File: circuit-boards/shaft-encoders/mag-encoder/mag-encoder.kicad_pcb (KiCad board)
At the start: 4 copper layers, 26.7 x 31.8 mm, 23 parts, among them J1 0015912055, J2 CONFIG, U1 AP2120N-3.3TRG1, U2 SN74LVC1G02DBVR, U3 MA732GQ

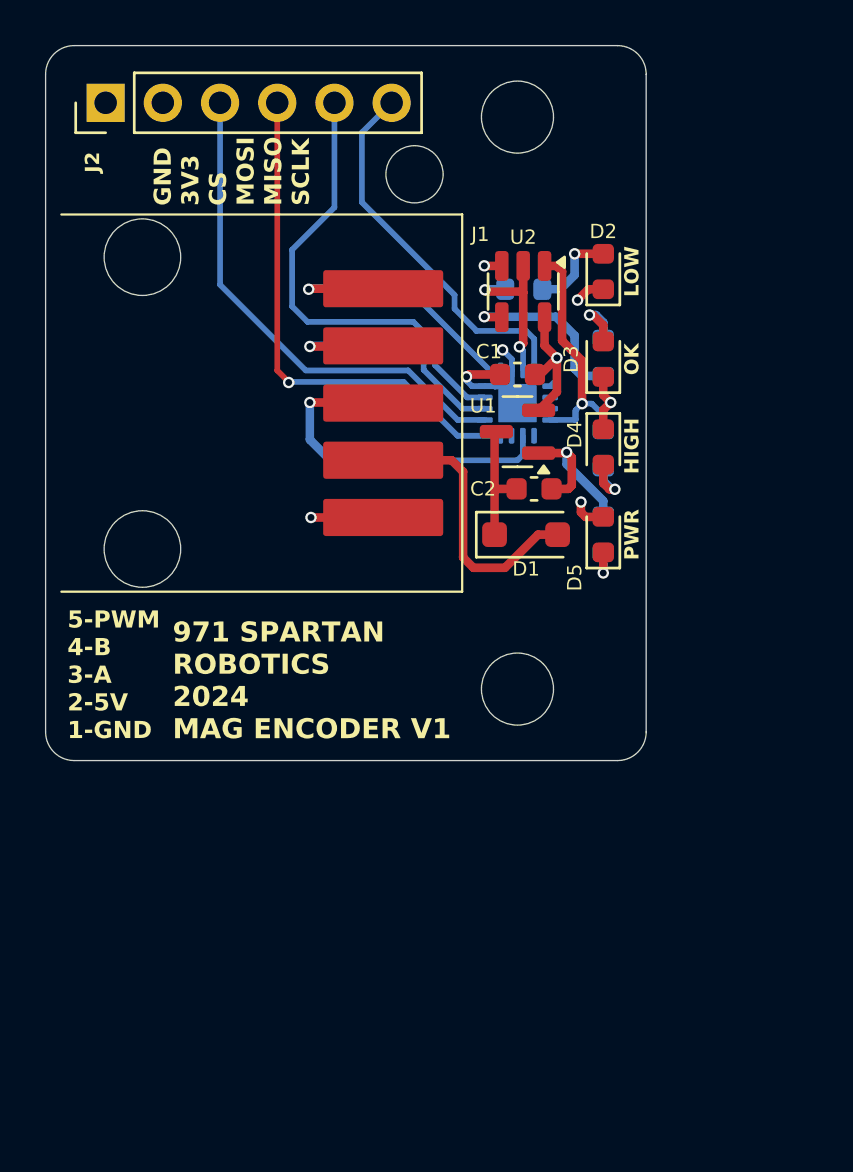
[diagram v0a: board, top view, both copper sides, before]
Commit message: checkin of mag encoder
Signed-off-by: Scott <sgberman1@gmail.com>
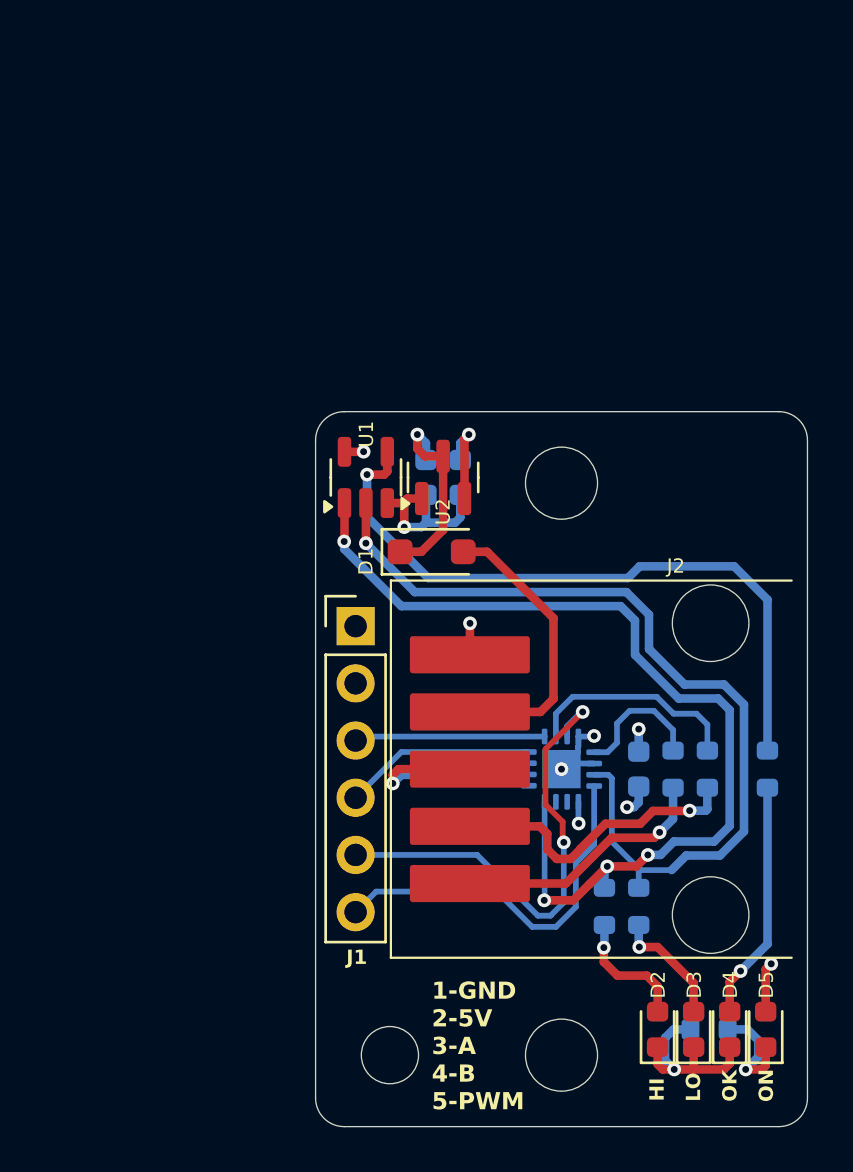
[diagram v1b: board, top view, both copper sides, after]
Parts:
- removed the H4 at (224.0, 117.5)
- removed the R3 at (232.4, 113.1)
- added C1: 1uF-10%-25V-0603, Capacitor_SMD:C_0603_1608Metric, B.Cu at (226.1, 110.6)
- added H2: Slot, mag-encoder:pin-0.100, F.Cu at (238.2, 110.9)
- added R7: 1.00k-1%-0603, Resistor_SMD:R_0603_1608Metric, B.Cu at (237.1, 135.1)
- C2: moved to B.Cu
- C3: renamed from C1; moved to B.Cu
- D2: renamed from D4; value HIGH -> HI
- D3: renamed from D2; value LOW -> LO
- D5: value PWR -> ON
- moved H4 41.7 mm to (230.6, 136.3), turned to 180 degrees
- moved H3 39.1 mm to (222.9, 136.3)
- moved J2 37.5 mm to (241.5, 123.6), turned to 90 degrees
- moved D3 33.9 mm to (236.4, 135.1)
- moved D4 30.3 mm to (238.0, 135.1)
- moved R5 27.9 mm to (234.0, 129.7), turned to -90 degrees
- moved D2 26.0 mm to (234.8, 135.1), turned to 90 degrees
- moved J1 25.8 mm to (221.4, 117.2), turned to 0 degrees
- moved R3 25.1 mm to (235.5, 123.6), turned to -90 degrees
- moved R2 23.9 mm to (237.0, 123.6), turned to -90 degrees
- moved D5 23.1 mm to (239.6, 135.1)
- moved R6 20.3 mm to (232.5, 129.7)
- moved R1 19.7 mm to (239.7, 123.6), turned to -90 degrees
- moved C3 18.3 mm to (234.0, 123.6), turned to 90 degrees
- moved U3 16.4 mm to (230.6, 123.6), turned to 0 degrees
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- renumbered D3 to D4, H2 to H1, H1 to H4, J2 to J1, J1 to J2, R6 to R2, R5 to R3, R7 to R4, R4 to R5, R2 to R6, U2 to U1, U1 to U2
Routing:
- net Net-(U3-MGL): track 7.45 -> 39.7 mm, vias 2 -> 1
- net Net-(U3-MGH): track 11.3 -> 43.2 mm, vias 1 -> 4
- net Net-(R1-Pad1): track 8.02 -> 30.1 mm
- net /MOSI: track 23.0 -> 8.54 mm, vias 1 -> 0
- net /CS: track 22.3 -> 8.47 mm
- net /B: track 5.32 -> 13.4 mm
- net Net-(D4-A): track 2.99 -> 10.6 mm
- net /PWM: track 5.42 -> 11.6 mm
- net Net-(U3-A): track 6.71 -> 1.92 mm
- net Net-(U3-B): track 5.53 -> 9.72 mm
- net +5V: track 5.59 -> 8.79 mm, vias 0 -> 1
- net Net-(D5-K): track 1.82 -> 4.86 mm
- net Net-(D2-A): track 2.72 -> 5.61 mm
- net Net-(D3-A): track 3.91 -> 5.33 mm
- net /MISO: track 20.6 -> 21.5 mm, vias 0 -> 2
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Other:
- board size 26.7 x 31.8 mm -> 21.8 x 31.8 mm
- board text added: "1-GND 2-5V 3-A 4-B 5-PWM"
- board text added: "3V3"
- board text added: "860.00 mils x 1250.00 mils"
- board text added: "CS"
- board text added: "GND"
- board text added: "MAG ENCODER V1 971 SPARTAN ROBOTICS 2024"
- board text added: "MISO"
- board text added: "MOSI"
- board text added: "SCLK"
- board text removed: "1050.00 mils x 1250.00 mils"
- board text removed: "5-PWM 4-B 3-A 2-5V 1-GND"
- board text removed: "971 SPARTAN ROBOTICS 2024 MAG ENCODER V1"
- board text removed: "GND 3V3 CS MOSI MISO SCLK"

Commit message: changed pins to 0.125".  Changed OK LED driver to mosfet.
Signed-off-by: Scott <sgberman1@gmail.com>
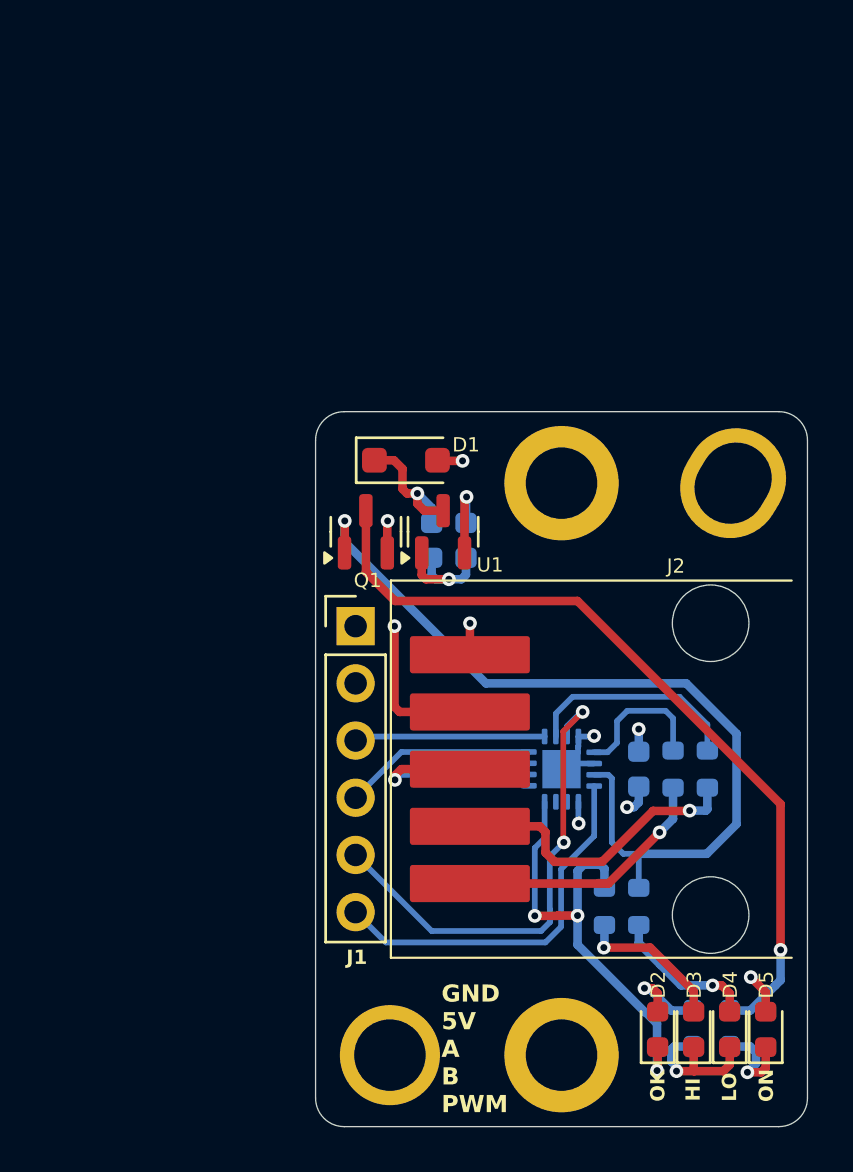
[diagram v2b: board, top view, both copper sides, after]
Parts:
- removed the U1 at (221.9, 110.6)
- added Q1: BSS84, Package_TO_SOT_SMD:SOT-23, F.Cu at (221.9, 113.0)
- moved R6 11.0 mm to (237.2, 134.3), turned to 180 degrees
- moved D1 4.22 mm to (223.6, 109.9)
- moved D2 3.20 mm to (234.8, 135.1)
- moved C1 2.81 mm to (226.3, 113.4)
- moved C2 2.81 mm to (224.8, 113.4)
- moved U1 2.41 mm to (225.3, 113.0)
- moved D3 1.60 mm to (236.4, 135.1)
- moved D4 1.60 mm to (238.0, 135.1)
- moved R7 0.77 mm to (237.2, 135.9)
- renumbered D4 to D2, D2 to D3, D3 to D4, R2 to R1, R3 to R2, R4 to R3, R5 to R4, R6 to R5, R1 to R6, U2 to U1, U3 to U2
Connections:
- D2 pad 1: GND -> Net-(D2-K)
- R5 pad 1: Net-(U3-MGH) -> Net-(D2-K)
- U2 pad 16: Net-(U3-MGH) -> Net-(D2-K)
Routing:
- net Net-(U3-MGH): track 43.2 -> 0.00 mm, vias 4 -> 0
- net Net-(D2-K): track 0.00 -> 20.8 mm, vias 0 -> 3
- net +5V_IN: track 12.8 -> 19.9 mm, vias 0 -> 2
- net Net-(D2-A): track 10.6 -> 4.05 mm
- net Net-(Q1-D): track 30.1 -> 36.0 mm
- net GND: track 22.8 -> 18.3 mm, vias 6 -> 5
- net +5V: track 8.79 -> 6.36 mm
- net Net-(D4-A): track 5.33 -> 6.58 mm
- net Net-(D3-A): track 5.61 -> 6.72 mm
- net Net-(Q1-G): track 39.7 -> 38.8 mm
- net Net-(D5-K): track 4.86 -> 4.12 mm
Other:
- board text added: "10.00 mils / 9.50 mils"
- board text added: "971 SPARTAN ROBOTICS 2024"
- board text added: "GND 5V A B PWM"
- board text added: "MAG ENCODER V1"
- board text added: "NOTES: 1. DO NOT INSTALL: J1"
- board text removed: "0.00 mils / 0.00 mils"
- board text removed: "1-GND 2-5V 3-A 4-B 5-PWM"
- board text removed: "MAG ENCODER V1 971 SPARTAN ROBOTICS 2024"
